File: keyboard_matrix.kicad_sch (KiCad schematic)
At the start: 282 parts, among them SW2000 MX-LED, SW2001 MX-LED, SW2002 F2, SW2003 F3, SW2004 F4, SW2005 F5, SW2006 F6, SW2007 F7, SW2008 F8, SW2009 F9, SW2010 F10, SW2011 F11, SW2012 F12, SW2013 PrtSc, SW2014 ScrLk, SW2015 Pause, SW2017 1, SW2018 2, SW2019 3, SW2020 4, SW2021 5, SW2022 6, SW2023 7, SW2024 8, SW2025 9, SW2026 0, SW2027 -, SW2028 =, SW2029 Bksp, SW2030 Ins, SW2031 Home, SW2032 PgUp, SW2033 NumLk, SW2034 /, SW2035 *, SW2036 -, SW2037 Tab, SW2038 Q, SW2039 W, SW2040 E, SW2041 R, SW2042 T, SW2043 Y, SW2044 U, SW2045 I, SW2046 O, SW2047 P, SW2048 [, SW2049 ], SW2050 \, SW2051 Del, SW2052 End, SW2053 PgDn, SW2054 7, SW2055 8, SW2056 9, SW2057 +, SW2058 Caps Lock, SW2059 A, SW2060 S, SW2061 D, SW2062 F, SW2063 G, SW2064 H, SW2065 J, SW2066 K, SW2067 L, SW2068 ;, SW2069 ', SW2070 Enter, SW2071 4, SW2072 5, SW2073 6, SW2074 Shift, SW2075 Z, SW2076 X, SW2077 C, SW2078 V, SW2079 B, SW2080 N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

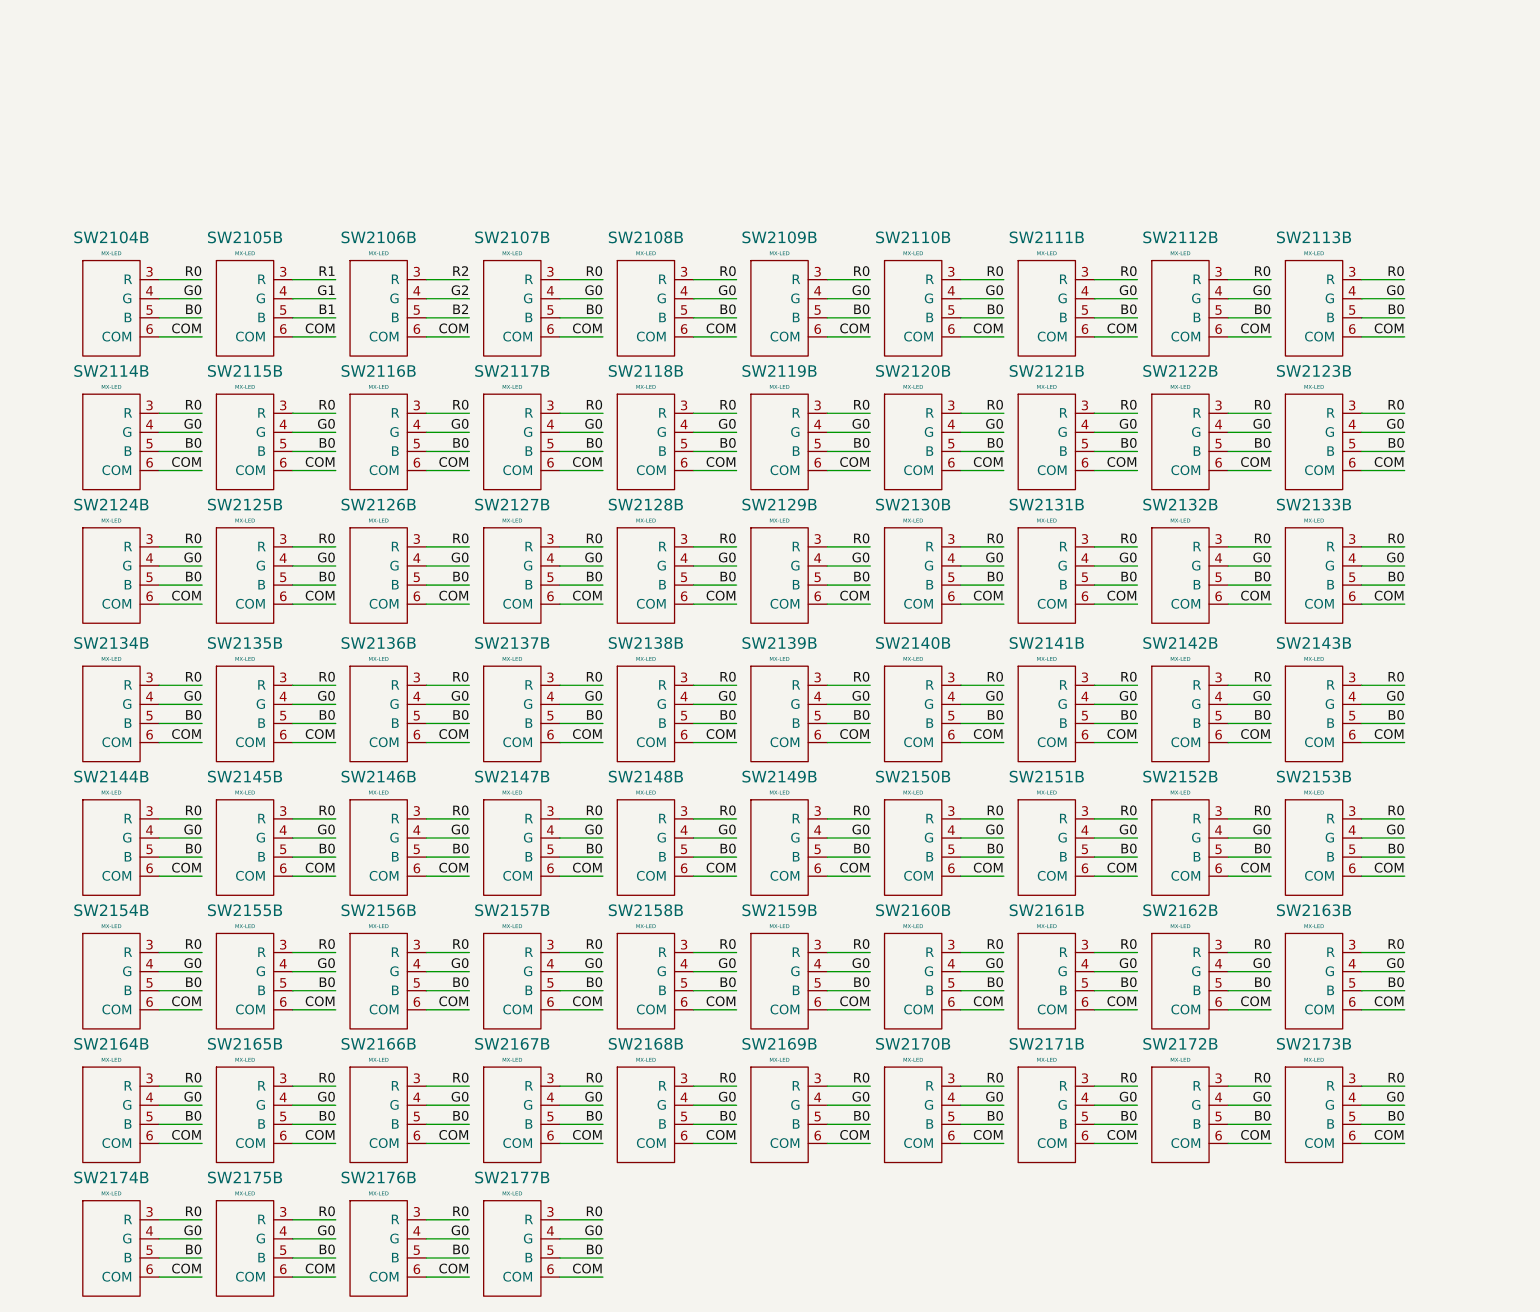
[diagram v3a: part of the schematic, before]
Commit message: Reset refdes for key LEDs
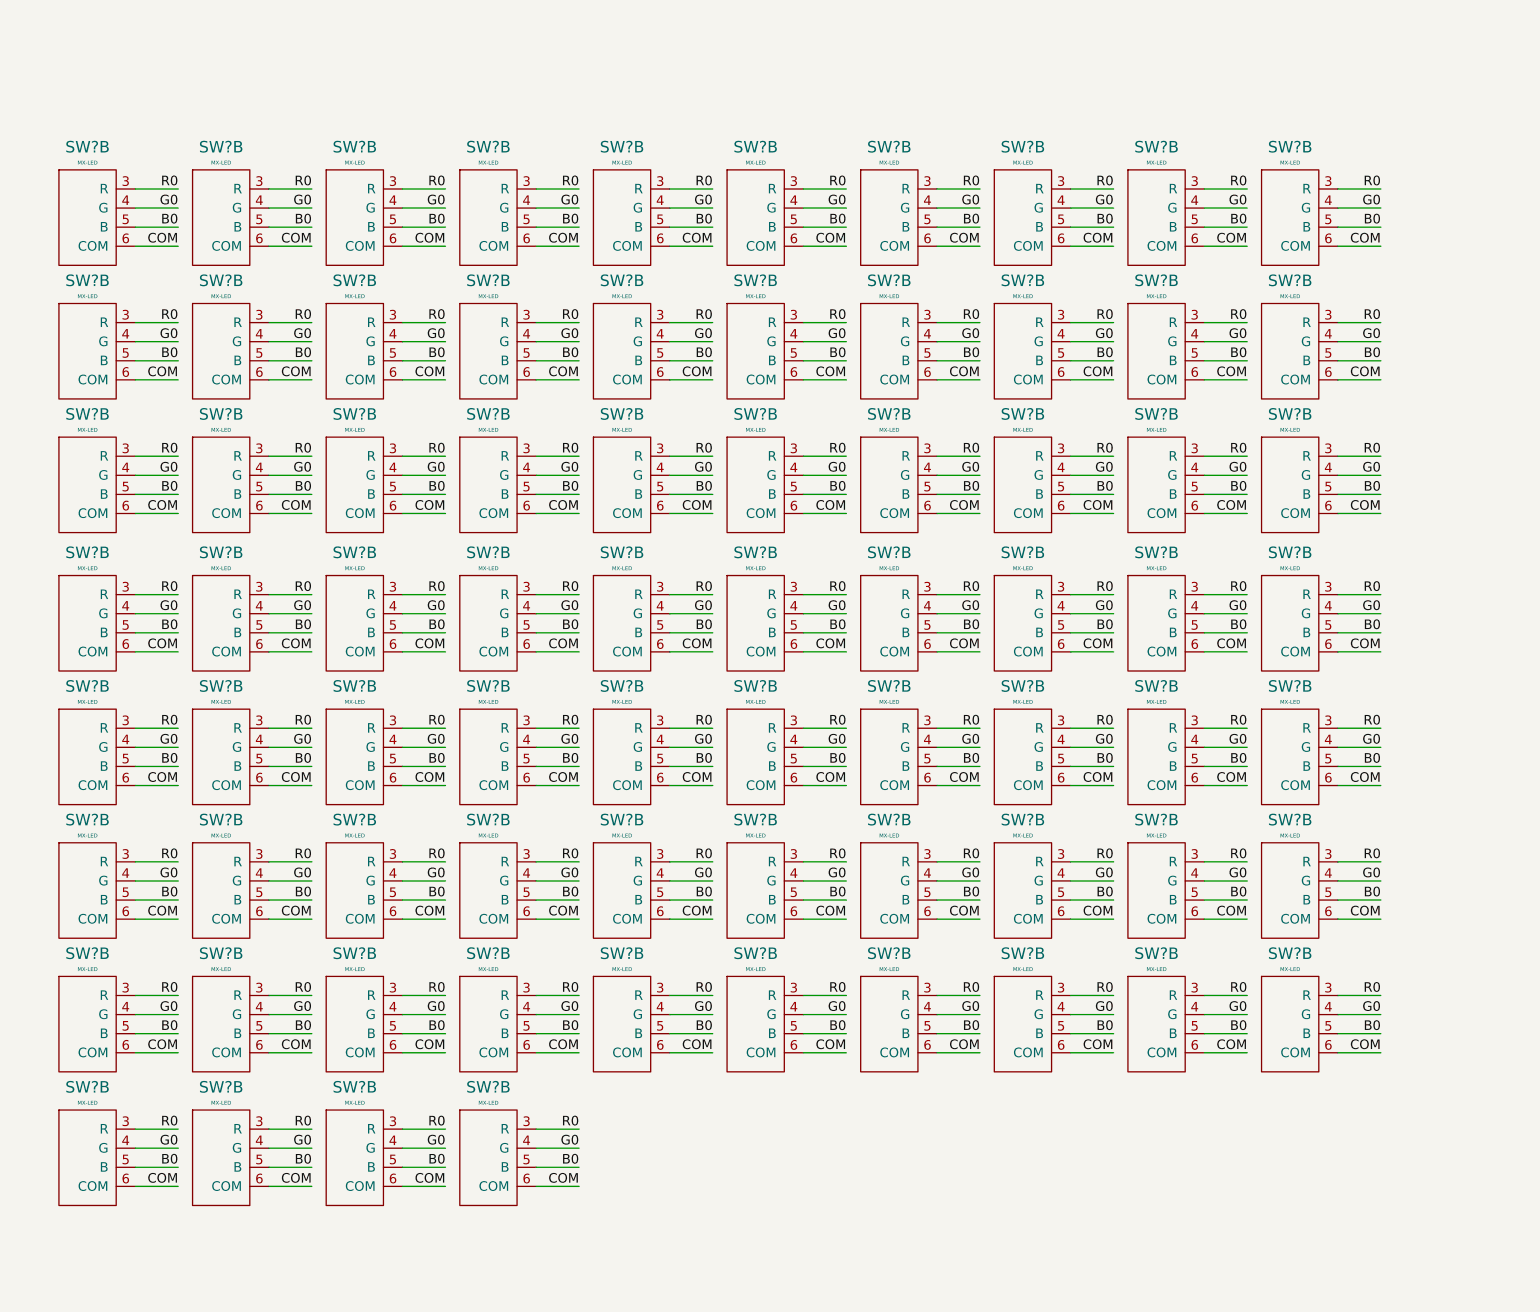
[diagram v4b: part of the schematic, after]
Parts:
- removed SW2104, SW2105, SW2106, SW2107, SW2108, SW2109, SW2110, SW2111, SW2112, SW2113, SW2114, SW2115, SW2116, SW2117, SW2118, SW2119, SW2120, SW2121, SW2122, SW2123, SW2124, SW2125, SW2126, SW2127, SW2128, SW2129, SW2130, SW2131, SW2132, SW2133, SW2134, SW2135, SW2136, SW2137, SW2138, SW2139, SW2140, SW2141, SW2142, SW2143, SW2144, SW2145, SW2146, SW2147, SW2148, SW2149, SW2150, SW2151, SW2152, SW2153, SW2154, SW2155, SW2156, SW2157, SW2158, SW2159, SW2160, SW2161, SW2162, SW2163, SW2164, SW2165, SW2166, SW2167, SW2168, SW2169, SW2170, SW2171, SW2172, SW2173, SW2174, SW2175, SW2176, SW2177: MX-LED, symbol Keyboard:MX-LED
- added SW? (x74): MX-LED, symbol Keyboard:MX-LED
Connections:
- net B0: now also SW?.5 (B), SW?.5 (B), SW?.5 (B), SW?.5 (B), SW?.5 (B), SW?.5 (B), SW?.5 (B), SW?.5 (B), SW?.5 (B), SW?.5 (B), SW?.5 (B), SW?.5 (B), SW?.5 (B), SW?.5 (B), SW?.5 (B), SW?.5 (B), SW?.5 (B), SW?.5 (B), SW?.5 (B), SW?.5 (B), SW?.5 (B), SW?.5 (B), SW?.5 (B), SW?.5 (B), SW?.5 (B), SW?.5 (B), SW?.5 (B), SW?.5 (B), SW?.5 (B), SW?.5 (B), SW?.5 (B), SW?.5 (B), SW?.5 (B), SW?.5 (B), SW?.5 (B), SW?.5 (B), SW?.5 (B), SW?.5 (B), SW?.5 (B), SW?.5 (B), SW?.5 (B), SW?.5 (B), SW?.5 (B), SW?.5 (B), SW?.5 (B), SW?.5 (B), SW?.5 (B), SW?.5 (B), SW?.5 (B), SW?.5 (B), SW?.5 (B), SW?.5 (B), SW?.5 (B), SW?.5 (B), SW?.5 (B), SW?.5 (B), SW?.5 (B), SW?.5 (B), SW?.5 (B), SW?.5 (B), SW?.5 (B), SW?.5 (B), SW?.5 (B), SW?.5 (B), SW?.5 (B), SW?.5 (B), SW?.5 (B), SW?.5 (B), SW?.5 (B), SW?.5 (B), SW?.5 (B), SW?.5 (B), SW?.5 (B), SW?.5 (B)
- net COM: now also SW?.6 (COM), SW?.6 (COM), SW?.6 (COM), SW?.6 (COM), SW?.6 (COM), SW?.6 (COM), SW?.6 (COM), SW?.6 (COM), SW?.6 (COM), SW?.6 (COM), SW?.6 (COM), SW?.6 (COM), SW?.6 (COM), SW?.6 (COM), SW?.6 (COM), SW?.6 (COM), SW?.6 (COM), SW?.6 (COM), SW?.6 (COM), SW?.6 (COM), SW?.6 (COM), SW?.6 (COM), SW?.6 (COM), SW?.6 (COM), SW?.6 (COM), SW?.6 (COM), SW?.6 (COM), SW?.6 (COM), SW?.6 (COM), SW?.6 (COM), SW?.6 (COM), SW?.6 (COM), SW?.6 (COM), SW?.6 (COM), SW?.6 (COM), SW?.6 (COM), SW?.6 (COM), SW?.6 (COM), SW?.6 (COM), SW?.6 (COM), SW?.6 (COM), SW?.6 (COM), SW?.6 (COM), SW?.6 (COM), SW?.6 (COM), SW?.6 (COM), SW?.6 (COM), SW?.6 (COM), SW?.6 (COM), SW?.6 (COM), SW?.6 (COM), SW?.6 (COM), SW?.6 (COM), SW?.6 (COM), SW?.6 (COM), SW?.6 (COM), SW?.6 (COM), SW?.6 (COM), SW?.6 (COM), SW?.6 (COM), SW?.6 (COM), SW?.6 (COM), SW?.6 (COM), SW?.6 (COM), SW?.6 (COM), SW?.6 (COM), SW?.6 (COM), SW?.6 (COM), SW?.6 (COM), SW?.6 (COM), SW?.6 (COM), SW?.6 (COM), SW?.6 (COM), SW?.6 (COM)
- net G0: now also SW?.4 (G), SW?.4 (G), SW?.4 (G), SW?.4 (G), SW?.4 (G), SW?.4 (G), SW?.4 (G), SW?.4 (G), SW?.4 (G), SW?.4 (G), SW?.4 (G), SW?.4 (G), SW?.4 (G), SW?.4 (G), SW?.4 (G), SW?.4 (G), SW?.4 (G), SW?.4 (G), SW?.4 (G), SW?.4 (G), SW?.4 (G), SW?.4 (G), SW?.4 (G), SW?.4 (G), SW?.4 (G), SW?.4 (G), SW?.4 (G), SW?.4 (G), SW?.4 (G), SW?.4 (G), SW?.4 (G), SW?.4 (G), SW?.4 (G), SW?.4 (G), SW?.4 (G), SW?.4 (G), SW?.4 (G), SW?.4 (G), SW?.4 (G), SW?.4 (G), SW?.4 (G), SW?.4 (G), SW?.4 (G), SW?.4 (G), SW?.4 (G), SW?.4 (G), SW?.4 (G), SW?.4 (G), SW?.4 (G), SW?.4 (G), SW?.4 (G), SW?.4 (G), SW?.4 (G), SW?.4 (G), SW?.4 (G), SW?.4 (G), SW?.4 (G), SW?.4 (G), SW?.4 (G), SW?.4 (G), SW?.4 (G), SW?.4 (G), SW?.4 (G), SW?.4 (G), SW?.4 (G), SW?.4 (G), SW?.4 (G), SW?.4 (G), SW?.4 (G), SW?.4 (G), SW?.4 (G), SW?.4 (G), SW?.4 (G), SW?.4 (G)
- net R0: now also SW?.3 (R), SW?.3 (R), SW?.3 (R), SW?.3 (R), SW?.3 (R), SW?.3 (R), SW?.3 (R), SW?.3 (R), SW?.3 (R), SW?.3 (R), SW?.3 (R), SW?.3 (R), SW?.3 (R), SW?.3 (R), SW?.3 (R), SW?.3 (R), SW?.3 (R), SW?.3 (R), SW?.3 (R), SW?.3 (R), SW?.3 (R), SW?.3 (R), SW?.3 (R), SW?.3 (R), SW?.3 (R), SW?.3 (R), SW?.3 (R), SW?.3 (R), SW?.3 (R), SW?.3 (R), SW?.3 (R), SW?.3 (R), SW?.3 (R), SW?.3 (R), SW?.3 (R), SW?.3 (R), SW?.3 (R), SW?.3 (R), SW?.3 (R), SW?.3 (R), SW?.3 (R), SW?.3 (R), SW?.3 (R), SW?.3 (R), SW?.3 (R), SW?.3 (R), SW?.3 (R), SW?.3 (R), SW?.3 (R), SW?.3 (R), SW?.3 (R), SW?.3 (R), SW?.3 (R), SW?.3 (R), SW?.3 (R), SW?.3 (R), SW?.3 (R), SW?.3 (R), SW?.3 (R), SW?.3 (R), SW?.3 (R), SW?.3 (R), SW?.3 (R), SW?.3 (R), SW?.3 (R), SW?.3 (R), SW?.3 (R), SW?.3 (R), SW?.3 (R), SW?.3 (R), SW?.3 (R), SW?.3 (R), SW?.3 (R), SW?.3 (R)

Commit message: ifxme
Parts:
- removed SW? (x24): MX-LED, symbol Keyboard:MX-LED
- added SW? (x50): MX-LED, symbol Keyboard:MX-LED
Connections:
- net B0: now also SW?.5 (B); no longer SW?.5 (B), SW?.5 (B), SW?.5 (B), SW?.5 (B), SW?.5 (B), SW?.5 (B), SW?.5 (B), SW?.5 (B), SW?.5 (B), SW?.5 (B), SW?.5 (B), SW?.5 (B), SW?.5 (B), SW?.5 (B), SW?.5 (B), SW?.5 (B), SW?.5 (B), SW?.5 (B), SW?.5 (B), SW?.5 (B), SW?.5 (B), SW?.5 (B), SW?.5 (B), SW?.5 (B), SW?.5 (B), SW?.5 (B), SW?.5 (B), SW?.5 (B), SW?.5 (B), SW?.5 (B), SW?.5 (B), SW?.5 (B), SW?.5 (B), SW?.5 (B), SW?.5 (B), SW?.5 (B), SW?.5 (B), SW?.5 (B), SW?.5 (B), SW?.5 (B), SW?.5 (B), SW?.5 (B), SW?.5 (B), SW?.5 (B), SW?.5 (B), SW?.5 (B), SW?.5 (B), SW?.5 (B), SW?.5 (B)
- net COM: now also SW?.6 (COM), SW?.6 (COM), SW?.6 (COM), SW?.6 (COM), SW?.6 (COM), SW?.6 (COM), SW?.6 (COM), SW?.6 (COM), SW?.6 (COM), SW?.6 (COM), SW?.6 (COM), SW?.6 (COM), SW?.6 (COM), SW?.6 (COM), SW?.6 (COM), SW?.6 (COM), SW?.6 (COM), SW?.6 (COM), SW?.6 (COM), SW?.6 (COM), SW?.6 (COM), SW?.6 (COM), SW?.6 (COM), SW?.6 (COM), SW?.6 (COM), SW?.6 (COM), SW?.6 (COM), SW?.6 (COM), SW?.6 (COM), SW?.6 (COM), SW?.6 (COM), SW?.6 (COM), SW?.6 (COM), SW?.6 (COM), SW?.6 (COM), SW?.6 (COM), SW?.6 (COM), SW?.6 (COM), SW?.6 (COM), SW?.6 (COM), SW?.6 (COM), SW?.6 (COM), SW?.6 (COM), SW?.6 (COM), SW?.6 (COM), SW?.6 (COM), SW?.6 (COM), SW?.6 (COM), SW?.6 (COM), SW?.6 (COM)
- net G0: now also SW?.4 (G); no longer SW?.4 (G), SW?.4 (G), SW?.4 (G), SW?.4 (G), SW?.4 (G), SW?.4 (G), SW?.4 (G), SW?.4 (G), SW?.4 (G), SW?.4 (G), SW?.4 (G), SW?.4 (G), SW?.4 (G), SW?.4 (G), SW?.4 (G), SW?.4 (G), SW?.4 (G), SW?.4 (G), SW?.4 (G), SW?.4 (G), SW?.4 (G), SW?.4 (G), SW?.4 (G), SW?.4 (G), SW?.4 (G), SW?.4 (G), SW?.4 (G), SW?.4 (G), SW?.4 (G), SW?.4 (G), SW?.4 (G), SW?.4 (G), SW?.4 (G), SW?.4 (G), SW?.4 (G), SW?.4 (G), SW?.4 (G), SW?.4 (G), SW?.4 (G), SW?.4 (G), SW?.4 (G), SW?.4 (G), SW?.4 (G), SW?.4 (G), SW?.4 (G), SW?.4 (G), SW?.4 (G), SW?.4 (G), SW?.4 (G)
- net R0: now also SW?.3 (R); no longer SW?.3 (R), SW?.3 (R), SW?.3 (R), SW?.3 (R), SW?.3 (R), SW?.3 (R), SW?.3 (R), SW?.3 (R), SW?.3 (R), SW?.3 (R), SW?.3 (R), SW?.3 (R), SW?.3 (R), SW?.3 (R), SW?.3 (R), SW?.3 (R), SW?.3 (R), SW?.3 (R), SW?.3 (R), SW?.3 (R), SW?.3 (R), SW?.3 (R), SW?.3 (R), SW?.3 (R), SW?.3 (R), SW?.3 (R), SW?.3 (R), SW?.3 (R), SW?.3 (R), SW?.3 (R), SW?.3 (R), SW?.3 (R), SW?.3 (R), SW?.3 (R), SW?.3 (R), SW?.3 (R), SW?.3 (R), SW?.3 (R), SW?.3 (R), SW?.3 (R), SW?.3 (R), SW?.3 (R), SW?.3 (R), SW?.3 (R), SW?.3 (R), SW?.3 (R), SW?.3 (R), SW?.3 (R), SW?.3 (R)
- new net B1: SW?.5 (B), SW?.5 (B)
- new net B10: SW?.5 (B), SW?.5 (B)
- new net B11: SW?.5 (B), SW?.5 (B)
- new net B12: SW?.5 (B), SW?.5 (B)
- new net B13: SW?.5 (B), SW?.5 (B)
- new net B14: SW?.5 (B), SW?.5 (B)
- new net B15: SW?.5 (B), SW?.5 (B)
- new net B16: SW?.5 (B), SW?.5 (B)
- new net B17: SW?.5 (B), SW?.5 (B)
- new net B18: SW?.5 (B), SW?.5 (B)
- new net B19: SW?.5 (B), SW?.5 (B)
- new net B2: SW?.5 (B), SW?.5 (B)
- new net B20: SW?.5 (B), SW?.5 (B)
- new net B21: SW?.5 (B), SW?.5 (B)
- new net B22: SW?.5 (B), SW?.5 (B)
- new net B23: SW?.5 (B), SW?.5 (B)
- new net B24: SW?.5 (B), SW?.5 (B)
- new net B25: SW?.5 (B), SW?.5 (B)
- new net B26: SW?.5 (B), SW?.5 (B)
- new net B27: SW?.5 (B), SW?.5 (B)
- new net B28: SW?.5 (B), SW?.5 (B)
- new net B29: SW?.5 (B), SW?.5 (B)
- new net B3: SW?.5 (B), SW?.5 (B)
- new net B30: SW?.5 (B), SW?.5 (B)
- new net B31: SW?.5 (B), SW?.5 (B)
- new net B32: SW?.5 (B), SW?.5 (B)
- new net B33: SW?.5 (B), SW?.5 (B)
- new net B34: SW?.5 (B), SW?.5 (B)
- new net B35: SW?.5 (B), SW?.5 (B)
- new net B36: SW?.5 (B), SW?.5 (B)
- new net B37: SW?.5 (B), SW?.5 (B)
- new net B38: SW?.5 (B), SW?.5 (B)
- new net B39: SW?.5 (B), SW?.5 (B)
- new net B4: SW?.5 (B), SW?.5 (B)
- new net B40: SW?.5 (B), SW?.5 (B)
- new net B41: SW?.5 (B), SW?.5 (B)
- new net B42: SW?.5 (B), SW?.5 (B)
- new net B43: SW?.5 (B), SW?.5 (B)
- new net B44: SW?.5 (B), SW?.5 (B)
- new net B45: SW?.5 (B), SW?.5 (B)
- new net B46: SW?.5 (B), SW?.5 (B)
- new net B47: SW?.5 (B), SW?.5 (B)
- new net B48: SW?.5 (B), SW?.5 (B)
- new net B49: SW?.5 (B), SW?.5 (B)
- new net B5: SW?.5 (B), SW?.5 (B)
- new net B6: SW?.5 (B), SW?.5 (B)
- new net B7: SW?.5 (B), SW?.5 (B)
- new net B8: SW?.5 (B), SW?.5 (B)
- new net B9: SW?.5 (B), SW?.5 (B)
- new net G1: SW?.4 (G), SW?.4 (G)
- new net G10: SW?.4 (G), SW?.4 (G)
- new net G11: SW?.4 (G), SW?.4 (G)
- new net G12: SW?.4 (G), SW?.4 (G)
- new net G13: SW?.4 (G), SW?.4 (G)
- new net G14: SW?.4 (G), SW?.4 (G)
- new net G15: SW?.4 (G), SW?.4 (G)
- new net G16: SW?.4 (G), SW?.4 (G)
- new net G17: SW?.4 (G), SW?.4 (G)
- new net G18: SW?.4 (G), SW?.4 (G)
- new net G19: SW?.4 (G), SW?.4 (G)
- new net G2: SW?.4 (G), SW?.4 (G)
- new net G20: SW?.4 (G), SW?.4 (G)
- new net G21: SW?.4 (G), SW?.4 (G)
- new net G22: SW?.4 (G), SW?.4 (G)
- new net G23: SW?.4 (G), SW?.4 (G)
- new net G24: SW?.4 (G), SW?.4 (G)
- new net G25: SW?.4 (G), SW?.4 (G)
- new net G26: SW?.4 (G), SW?.4 (G)
- new net G27: SW?.4 (G), SW?.4 (G)
- new net G28: SW?.4 (G), SW?.4 (G)
- new net G29: SW?.4 (G), SW?.4 (G)
- new net G3: SW?.4 (G), SW?.4 (G)
- new net G30: SW?.4 (G), SW?.4 (G)
- new net G31: SW?.4 (G), SW?.4 (G)
- new net G32: SW?.4 (G), SW?.4 (G)
- new net G33: SW?.4 (G), SW?.4 (G)
- new net G34: SW?.4 (G), SW?.4 (G)
- new net G35: SW?.4 (G), SW?.4 (G)
- new net G36: SW?.4 (G), SW?.4 (G)
- new net G37: SW?.4 (G), SW?.4 (G)
- new net G38: SW?.4 (G), SW?.4 (G)
- new net G39: SW?.4 (G), SW?.4 (G)
- new net G4: SW?.4 (G), SW?.4 (G)
- new net G40: SW?.4 (G), SW?.4 (G)
- new net G41: SW?.4 (G), SW?.4 (G)
- new net G42: SW?.4 (G), SW?.4 (G)
- new net G43: SW?.4 (G), SW?.4 (G)
- new net G44: SW?.4 (G), SW?.4 (G)
- new net G45: SW?.4 (G), SW?.4 (G)
- new net G46: SW?.4 (G), SW?.4 (G)
- new net G47: SW?.4 (G), SW?.4 (G)
- new net G48: SW?.4 (G), SW?.4 (G)
- new net G49: SW?.4 (G), SW?.4 (G)
- new net G5: SW?.4 (G), SW?.4 (G)
- new net G6: SW?.4 (G), SW?.4 (G)
- new net G7: SW?.4 (G), SW?.4 (G)
- new net G8: SW?.4 (G), SW?.4 (G)
- new net G9: SW?.4 (G), SW?.4 (G)
- new net R1: SW?.3 (R), SW?.3 (R)
- new net R10: SW?.3 (R), SW?.3 (R)
- new net R11: SW?.3 (R), SW?.3 (R)
- new net R12: SW?.3 (R), SW?.3 (R)
- new net R13: SW?.3 (R), SW?.3 (R)
- new net R14: SW?.3 (R), SW?.3 (R)
- new net R15: SW?.3 (R), SW?.3 (R)
- new net R16: SW?.3 (R), SW?.3 (R)
- new net R17: SW?.3 (R), SW?.3 (R)
- new net R18: SW?.3 (R), SW?.3 (R)
- new net R19: SW?.3 (R), SW?.3 (R)
- new net R2: SW?.3 (R), SW?.3 (R)
- new net R20: SW?.3 (R), SW?.3 (R)
- new net R21: SW?.3 (R), SW?.3 (R)
- new net R22: SW?.3 (R), SW?.3 (R)
- new net R23: SW?.3 (R), SW?.3 (R)
- new net R24: SW?.3 (R), SW?.3 (R)
- new net R25: SW?.3 (R), SW?.3 (R)
- new net R26: SW?.3 (R), SW?.3 (R)
- new net R27: SW?.3 (R), SW?.3 (R)
- new net R28: SW?.3 (R), SW?.3 (R)
- new net R29: SW?.3 (R), SW?.3 (R)
- new net R3: SW?.3 (R), SW?.3 (R)
- new net R30: SW?.3 (R), SW?.3 (R)
- new net R31: SW?.3 (R), SW?.3 (R)
- new net R32: SW?.3 (R), SW?.3 (R)
- new net R33: SW?.3 (R), SW?.3 (R)
- new net R34: SW?.3 (R), SW?.3 (R)
- new net R35: SW?.3 (R), SW?.3 (R)
- new net R36: SW?.3 (R), SW?.3 (R)
- new net R37: SW?.3 (R), SW?.3 (R)
- new net R38: SW?.3 (R), SW?.3 (R)
- new net R39: SW?.3 (R), SW?.3 (R)
- new net R4: SW?.3 (R), SW?.3 (R)
- new net R40: SW?.3 (R), SW?.3 (R)
- new net R41: SW?.3 (R), SW?.3 (R)
- new net R42: SW?.3 (R), SW?.3 (R)
- new net R43: SW?.3 (R), SW?.3 (R)
- new net R44: SW?.3 (R), SW?.3 (R)
- new net R45: SW?.3 (R), SW?.3 (R)
- new net R46: SW?.3 (R), SW?.3 (R)
- new net R47: SW?.3 (R), SW?.3 (R)
- new net R48: SW?.3 (R), SW?.3 (R)
- new net R49: SW?.3 (R), SW?.3 (R)
- new net R5: SW?.3 (R), SW?.3 (R)
- new net R6: SW?.3 (R), SW?.3 (R)
- new net R7: SW?.3 (R), SW?.3 (R)
- new net R8: SW?.3 (R), SW?.3 (R)
- new net R9: SW?.3 (R), SW?.3 (R)

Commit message: fixme
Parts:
- added SW2204, SW2205, SW2206, SW2207: MX-LED, symbol Keyboard:MX-LED
- gave numbers to parts that had none: 100
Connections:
- net B0: no longer SW2154.5 (B)
- net B1: no longer SW2155.5 (B)
- net B10: no longer SW2164.5 (B)
- net B11: no longer SW2165.5 (B)
- net B12: no longer SW2166.5 (B)
- net B13: no longer SW2167.5 (B)
- net B14: no longer SW2168.5 (B)
- net B15: no longer SW2169.5 (B)
- net B16: no longer SW2170.5 (B)
- net B17: no longer SW2171.5 (B)
- net B18: no longer SW2172.5 (B)
- net B19: no longer SW2173.5 (B)
- net B2: no longer SW2156.5 (B)
- net B20: no longer SW2174.5 (B)
- net B21: no longer SW2175.5 (B)
- net B22: no longer SW2176.5 (B)
- net B23: no longer SW2177.5 (B)
- net B24: no longer SW2178.5 (B)
- net B25: no longer SW2179.5 (B)
- net B26: no longer SW2180.5 (B)
- net B27: no longer SW2181.5 (B)
- net B28: no longer SW2182.5 (B)
- net B29: no longer SW2183.5 (B)
- net B3: no longer SW2157.5 (B)
- net B30: no longer SW2184.5 (B)
- net B31: no longer SW2185.5 (B)
- net B32: no longer SW2186.5 (B)
- net B33: no longer SW2187.5 (B)
- net B34: no longer SW2188.5 (B)
- net B35: no longer SW2189.5 (B)
- net B36: no longer SW2190.5 (B)
- net B37: no longer SW2191.5 (B)
- net B38: no longer SW2192.5 (B)
- net B39: no longer SW2193.5 (B)
- net B4: no longer SW2158.5 (B)
- net B40: no longer SW2194.5 (B)
- net B41: no longer SW2195.5 (B)
- net B42: no longer SW2196.5 (B)
- net B43: no longer SW2197.5 (B)
- net B44: no longer SW2198.5 (B)
- net B45: no longer SW2199.5 (B)
- net B46: no longer SW2200.5 (B)
- net B47: no longer SW2201.5 (B)
- net B48: no longer SW2202.5 (B)
- net B49: no longer SW2203.5 (B)
- net B5: no longer SW2159.5 (B)
- net B6: no longer SW2160.5 (B)
- net B7: no longer SW2161.5 (B)
- net B8: no longer SW2162.5 (B)
- net B9: no longer SW2163.5 (B)
- net COM: now also SW2204.6 (COM), SW2205.6 (COM), SW2206.6 (COM), SW2207.6 (COM)
- net G0: no longer SW2154.4 (G)
- net G1: no longer SW2155.4 (G)
- net G10: no longer SW2164.4 (G)
- net G11: no longer SW2165.4 (G)
- net G12: no longer SW2166.4 (G)
- net G13: no longer SW2167.4 (G)
- net G14: no longer SW2168.4 (G)
- net G15: no longer SW2169.4 (G)
- net G16: no longer SW2170.4 (G)
- net G17: no longer SW2171.4 (G)
- net G18: no longer SW2172.4 (G)
- net G19: no longer SW2173.4 (G)
- net G2: no longer SW2156.4 (G)
- net G20: no longer SW2174.4 (G)
- net G21: no longer SW2175.4 (G)
- net G22: no longer SW2176.4 (G)
- net G23: no longer SW2177.4 (G)
- net G24: no longer SW2178.4 (G)
- net G25: no longer SW2179.4 (G)
- net G26: no longer SW2180.4 (G)
- net G27: no longer SW2181.4 (G)
- net G28: no longer SW2182.4 (G)
- net G29: no longer SW2183.4 (G)
- net G3: no longer SW2157.4 (G)
- net G30: no longer SW2184.4 (G)
- net G31: no longer SW2185.4 (G)
- net G32: no longer SW2186.4 (G)
- net G33: no longer SW2187.4 (G)
- net G34: no longer SW2188.4 (G)
- net G35: no longer SW2189.4 (G)
- net G36: no longer SW2190.4 (G)
- net G37: no longer SW2191.4 (G)
- net G38: no longer SW2192.4 (G)
- net G39: no longer SW2193.4 (G)
- net G4: no longer SW2158.4 (G)
- net G40: no longer SW2194.4 (G)
- net G41: no longer SW2195.4 (G)
- net G42: no longer SW2196.4 (G)
- net G43: no longer SW2197.4 (G)
- net G44: no longer SW2198.4 (G)
- net G45: no longer SW2199.4 (G)
- net G46: no longer SW2200.4 (G)
- net G47: no longer SW2201.4 (G)
- net G48: no longer SW2202.4 (G)
- net G49: no longer SW2203.4 (G)
- net G5: no longer SW2159.4 (G)
- net G6: no longer SW2160.4 (G)
- net G7: no longer SW2161.4 (G)
- net G8: no longer SW2162.4 (G)
- net G9: no longer SW2163.4 (G)
- net R0: no longer SW2154.3 (R)
- net R1: no longer SW2155.3 (R)
- net R10: no longer SW2164.3 (R)
- net R11: no longer SW2165.3 (R)
- net R12: no longer SW2166.3 (R)
- net R13: no longer SW2167.3 (R)
- net R14: no longer SW2168.3 (R)
- net R15: no longer SW2169.3 (R)
- net R16: no longer SW2170.3 (R)
- net R17: no longer SW2171.3 (R)
- net R18: no longer SW2172.3 (R)
- net R19: no longer SW2173.3 (R)
- net R2: no longer SW2156.3 (R)
- net R20: no longer SW2174.3 (R)
- net R21: no longer SW2175.3 (R)
- net R22: no longer SW2176.3 (R)
- net R23: no longer SW2177.3 (R)
- net R24: no longer SW2178.3 (R)
- net R25: no longer SW2179.3 (R)
- net R26: no longer SW2180.3 (R)
- net R27: no longer SW2181.3 (R)
- net R28: no longer SW2182.3 (R)
- net R29: no longer SW2183.3 (R)
- net R3: no longer SW2157.3 (R)
- net R30: no longer SW2184.3 (R)
- net R31: no longer SW2185.3 (R)
- net R32: no longer SW2186.3 (R)
- net R33: no longer SW2187.3 (R)
- net R34: no longer SW2188.3 (R)
- net R35: no longer SW2189.3 (R)
- net R36: no longer SW2190.3 (R)
- net R37: no longer SW2191.3 (R)
- net R38: no longer SW2192.3 (R)
- net R39: no longer SW2193.3 (R)
- net R4: no longer SW2158.3 (R)
- net R40: no longer SW2194.3 (R)
- net R41: no longer SW2195.3 (R)
- net R42: no longer SW2196.3 (R)
- net R43: no longer SW2197.3 (R)
- net R44: no longer SW2198.3 (R)
- net R45: no longer SW2199.3 (R)
- net R46: no longer SW2200.3 (R)
- net R47: no longer SW2201.3 (R)
- net R48: no longer SW2202.3 (R)
- net R49: no longer SW2203.3 (R)
- net R5: no longer SW2159.3 (R)
- net R6: no longer SW2160.3 (R)
- net R7: no longer SW2161.3 (R)
- net R8: no longer SW2162.3 (R)
- net R9: no longer SW2163.3 (R)
- new net B100: SW2204.5 (B)
- new net B101: SW2205.5 (B)
- new net B102: SW2206.5 (B)
- new net B103: SW2207.5 (B)
- new net B50: SW2154.5 (B)
- new net B51: SW2155.5 (B)
- new net B52: SW2156.5 (B)
- new net B53: SW2157.5 (B)
- new net B54: SW2158.5 (B)
- new net B55: SW2159.5 (B)
- new net B56: SW2160.5 (B)
- new net B57: SW2161.5 (B)
- new net B58: SW2162.5 (B)
- new net B59: SW2163.5 (B)
- new net B60: SW2164.5 (B)
- new net B61: SW2165.5 (B)
- new net B62: SW2166.5 (B)
- new net B63: SW2167.5 (B)
- new net B64: SW2168.5 (B)
- new net B65: SW2169.5 (B)
- new net B66: SW2170.5 (B)
- new net B67: SW2171.5 (B)
- new net B68: SW2172.5 (B)
- new net B69: SW2173.5 (B)
- new net B70: SW2174.5 (B)
- new net B71: SW2175.5 (B)
- new net B72: SW2176.5 (B)
- new net B73: SW2177.5 (B)
- new net B74: SW2178.5 (B)
- new net B75: SW2179.5 (B)
- new net B76: SW2180.5 (B)
- new net B77: SW2181.5 (B)
- new net B78: SW2182.5 (B)
- new net B79: SW2183.5 (B)
- new net B80: SW2184.5 (B)
- new net B81: SW2185.5 (B)
- new net B82: SW2186.5 (B)
- new net B83: SW2187.5 (B)
- new net B84: SW2188.5 (B)
- new net B85: SW2189.5 (B)
- new net B86: SW2190.5 (B)
- new net B87: SW2191.5 (B)
- new net B88: SW2192.5 (B)
- new net B89: SW2193.5 (B)
- new net B90: SW2194.5 (B)
- new net B91: SW2195.5 (B)
- new net B92: SW2196.5 (B)
- new net B93: SW2197.5 (B)
- new net B94: SW2198.5 (B)
- new net B95: SW2199.5 (B)
- new net B96: SW2200.5 (B)
- new net B97: SW2201.5 (B)
- new net B98: SW2202.5 (B)
- new net B99: SW2203.5 (B)
- new net G100: SW2204.4 (G)
- new net G101: SW2205.4 (G)
- new net G102: SW2206.4 (G)
- new net G103: SW2207.4 (G)
- new net G50: SW2154.4 (G)
- new net G51: SW2155.4 (G)
- new net G52: SW2156.4 (G)
- new net G53: SW2157.4 (G)
- new net G54: SW2158.4 (G)
- new net G55: SW2159.4 (G)
- new net G56: SW2160.4 (G)
- new net G57: SW2161.4 (G)
- new net G58: SW2162.4 (G)
- new net G59: SW2163.4 (G)
- new net G60: SW2164.4 (G)
- new net G61: SW2165.4 (G)
- new net G62: SW2166.4 (G)
- new net G63: SW2167.4 (G)
- new net G64: SW2168.4 (G)
- new net G65: SW2169.4 (G)
- new net G66: SW2170.4 (G)
- new net G67: SW2171.4 (G)
- new net G68: SW2172.4 (G)
- new net G69: SW2173.4 (G)
- new net G70: SW2174.4 (G)
- new net G71: SW2175.4 (G)
- new net G72: SW2176.4 (G)
- new net G73: SW2177.4 (G)
- new net G74: SW2178.4 (G)
- new net G75: SW2179.4 (G)
- new net G76: SW2180.4 (G)
- new net G77: SW2181.4 (G)
- new net G78: SW2182.4 (G)
- new net G79: SW2183.4 (G)
- new net G80: SW2184.4 (G)
- new net G81: SW2185.4 (G)
- new net G82: SW2186.4 (G)
- new net G83: SW2187.4 (G)
- new net G84: SW2188.4 (G)
- new net G85: SW2189.4 (G)
- new net G86: SW2190.4 (G)
- new net G87: SW2191.4 (G)
- new net G88: SW2192.4 (G)
- new net G89: SW2193.4 (G)
- new net G90: SW2194.4 (G)
- new net G91: SW2195.4 (G)
- new net G92: SW2196.4 (G)
- new net G93: SW2197.4 (G)
- new net G94: SW2198.4 (G)
- new net G95: SW2199.4 (G)
- new net G96: SW2200.4 (G)
- new net G97: SW2201.4 (G)
- new net G98: SW2202.4 (G)
- new net G99: SW2203.4 (G)
- new net R100: SW2204.3 (R)
- new net R101: SW2205.3 (R)
- new net R102: SW2206.3 (R)
- new net R103: SW2207.3 (R)
- new net R50: SW2154.3 (R)
- new net R51: SW2155.3 (R)
- new net R52: SW2156.3 (R)
- new net R53: SW2157.3 (R)
- new net R54: SW2158.3 (R)
- new net R55: SW2159.3 (R)
- new net R56: SW2160.3 (R)
- new net R57: SW2161.3 (R)
- new net R58: SW2162.3 (R)
- new net R59: SW2163.3 (R)
- new net R60: SW2164.3 (R)
- new net R61: SW2165.3 (R)
- new net R62: SW2166.3 (R)
- new net R63: SW2167.3 (R)
- new net R64: SW2168.3 (R)
- new net R65: SW2169.3 (R)
- new net R66: SW2170.3 (R)
- new net R67: SW2171.3 (R)
- new net R68: SW2172.3 (R)
- new net R69: SW2173.3 (R)
- new net R70: SW2174.3 (R)
- new net R71: SW2175.3 (R)
- new net R72: SW2176.3 (R)
- new net R73: SW2177.3 (R)
- new net R74: SW2178.3 (R)
- new net R75: SW2179.3 (R)
- new net R76: SW2180.3 (R)
- new net R77: SW2181.3 (R)
- new net R78: SW2182.3 (R)
- new net R79: SW2183.3 (R)
- new net R80: SW2184.3 (R)
- new net R81: SW2185.3 (R)
- new net R82: SW2186.3 (R)
- new net R83: SW2187.3 (R)
- new net R84: SW2188.3 (R)
- new net R85: SW2189.3 (R)
- new net R86: SW2190.3 (R)
- new net R87: SW2191.3 (R)
- new net R88: SW2192.3 (R)
- new net R89: SW2193.3 (R)
- new net R90: SW2194.3 (R)
- new net R91: SW2195.3 (R)
- new net R92: SW2196.3 (R)
- new net R93: SW2197.3 (R)
- new net R94: SW2198.3 (R)
- new net R95: SW2199.3 (R)
- new net R96: SW2200.3 (R)
- new net R97: SW2201.3 (R)
- new net R98: SW2202.3 (R)
- new net R99: SW2203.3 (R)
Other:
- moved on the sheet: SW2104B, SW2105B, SW2106B, SW2107B, SW2108B, SW2109B, SW2110B, SW2111B, SW2112B, SW2113B, SW2114B, SW2115B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
